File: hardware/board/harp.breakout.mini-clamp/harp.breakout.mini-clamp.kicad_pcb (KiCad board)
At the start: 2 copper layers, 40 x 75 mm, 16 parts, among them J1 Conn_01x12_Socket, J5 Conn_02x10_Odd_Even, J6 Conn_01x12_Socket, U5 TXB0108

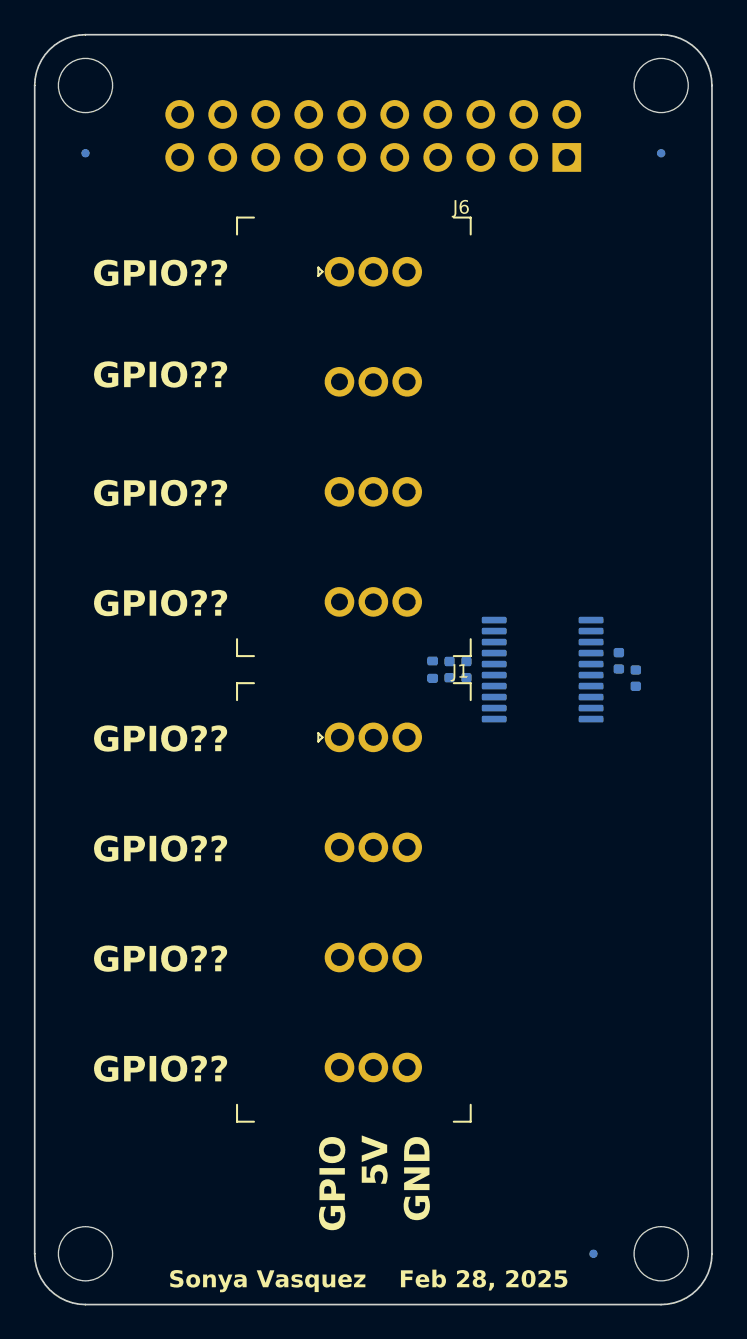
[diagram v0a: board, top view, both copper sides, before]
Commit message: route breakout board layout partially
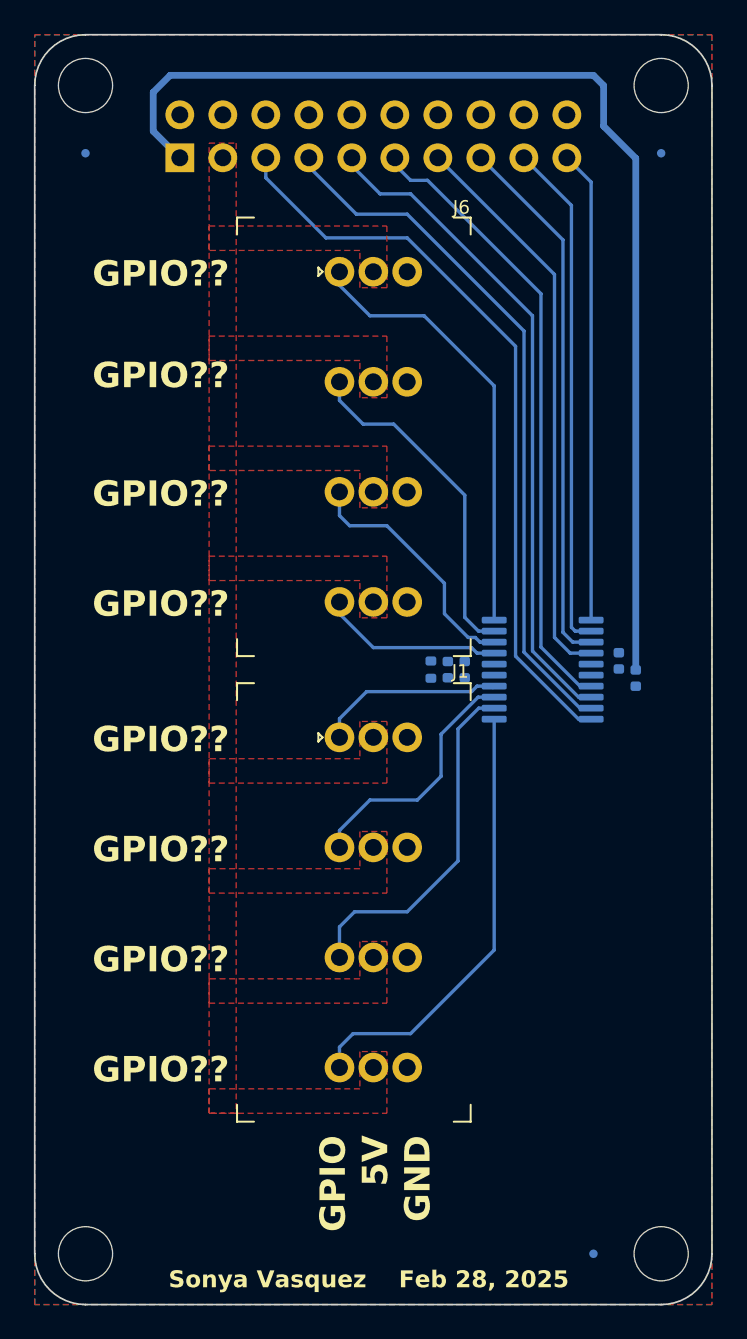
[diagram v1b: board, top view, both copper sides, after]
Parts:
- J5: footprint Connector_PinHeader_2.54mm:PinHeader_2x10_P2.54mm_Vertical -> Connector_PinSocket_2.54mm:PinSocket_2x10_P2.54mm_Vertical
- moved J5 22.9 mm to (128.6, 42.3), turned to -90 degrees
- moved C1 0.10 mm to (144.4, 72.5)
- moved C2 0.10 mm to (145.4, 72.5)
- moved R1 0.10 mm to (143.4, 72.5)
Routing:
- net +3.3V: track 0.00 -> 67.1 mm
- net /OUT3: track 0.00 -> 44.4 mm
- net /OUT2: track 0.00 -> 41.6 mm
- net /OUT1: track 0.00 -> 39.2 mm
- net /OUT0: track 0.00 -> 37.0 mm
- net /IN3: track 0.00 -> 33.7 mm
- net /IN2: track 0.00 -> 31.9 mm
- net /IN1: track 0.00 -> 30.1 mm
- net /IN0: track 0.00 -> 27.9 mm
- net /OUT3_5V: track 0.00 -> 26.4 mm
- net /IN0_5V: track 0.00 -> 26.2 mm
- net /OUT2_5V: track 0.00 -> 20.9 mm
- net /IN1_5V: track 0.00 -> 20.1 mm
- net /OUT1_5V: track 0.00 -> 14.9 mm
- net /IN2_5V: track 0.00 -> 14.7 mm
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- added copper zone on F.Cu, net +5V
- added copper zone on B.Cu, net GND
- added copper zone on F.Cu, net GND

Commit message: update breakout
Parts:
- added C5: 1uF, Capacitor_SMD:C_0402_1005Metric_Pad0.74x0.62mm_HandSolder, B.Cu at (155.0, 74.2)
- C1, C2, C3, C4: footprint Capacitor_SMD:C_0402_1005Metric -> Capacitor_SMD:C_0402_1005Metric_Pad0.74x0.62mm_HandSolder
- R1: footprint Resistor_SMD:R_0402_1005Metric -> Resistor_SMD:R_0402_1005Metric_Pad0.72x0.64mm_HandSolder
- moved FID2 61.0 mm to (123.0, 103.0)
- moved R1 11.6 mm to (155.0, 73.2), turned to 0 degrees
- moved C3 1.30 mm to (155.0, 71.8), turned to 180 degrees
- moved C4 1.28 mm to (155.0, 70.8), turned to 0 degrees
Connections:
- J1 pad 1: /OUT0_5V -> /IN3_5V
- J1 pad 10: /OUT3_5V -> /IN0_5V
- J1 pad 4: /OUT1_5V -> /IN2_5V
- J1 pad 7: /OUT2_5V -> /IN1_5V
- J5 pad 1: +3.3V -> /IN0
- J5 pad 11: /OUT0 -> /OUT1
- J5 pad 13: /IN3 -> /OUT2
- J5 pad 15: /IN2 -> /OUT3
- J5 pad 17: /IN1 -> +5V
- J5 pad 19: /IN0 -> +3.3V
- J5 pad 3: +5V -> /IN1
- J5 pad 5: /OUT3 -> /IN2
- J5 pad 7: /OUT2 -> /IN3
- J5 pad 9: /OUT1 -> /OUT0
- J6 pad 1: /IN0_5V -> /OUT3_5V
- J6 pad 10: /IN3_5V -> /OUT0_5V
- J6 pad 4: /IN1_5V -> /OUT2_5V
- J6 pad 7: /IN2_5V -> /OUT1_5V
- R1 pad 1: GND -> Net-(U5-OE)
- R1 pad 2: +5V -> +3.3V
- U5 pad 1: /IN0 -> /OUT3
- U5 pad 10: /OUT3 -> /IN0
- U5 pad 11: /OUT3_5V -> /IN0_5V
- U5 pad 12: /OUT2_5V -> /IN1_5V
- U5 pad 13: /OUT1_5V -> /IN2_5V
- U5 pad 14: /OUT0_5V -> /IN3_5V
- U5 pad 17: /IN3_5V -> /OUT0_5V
- U5 pad 18: /IN2_5V -> /OUT1_5V
- U5 pad 19: /IN1_5V -> /OUT2_5V
- U5 pad 2: /IN1 -> /OUT2
- U5 pad 20: /IN0_5V -> /OUT3_5V
- U5 pad 3: /IN2 -> /OUT1
- U5 pad 4: /IN3 -> /OUT0
- U5 pad 5: +3V3 -> +3.3V
- U5 pad 6: +3V3 -> Net-(U5-OE)
- U5 pad 7: /OUT0 -> /IN3
- U5 pad 8: /OUT1 -> /IN2
- U5 pad 9: /OUT2 -> /IN1
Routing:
- net +3.3V: track 67.1 -> 34.6 mm
- net /IN0: track 27.9 -> 49.5 mm
- net /IN1: track 30.1 -> 46.4 mm
- net /OUT3: track 44.4 -> 30.0 mm
- net /IN2: track 31.9 -> 43.8 mm
- net /OUT2: track 41.6 -> 32.4 mm
- net /IN3: track 33.7 -> 41.8 mm
- net /OUT1: track 39.2 -> 35.4 mm
- net GND: track 0.00 -> 3.51 mm, vias 0 -> 4
- net Net-(U5-OE): track 0.00 -> 2.85 mm
- net /OUT0: track 37.0 -> 38.1 mm
- net /OUT2_5V: track 20.9 -> 20.1 mm
- net +5V: vias 0 -> 2
- added copper zone on B.Cu, net +5V
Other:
- board text added: "0368-E-002-001.000.000"
- board text added: "AUX GPIO Breakout"
- board text added: "Sonya Vasquez Mar 3, 2025"
- board text removed: "GPIO??"
- board text removed: "Sonya Vasquez Feb 28, 2025"

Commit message: update breakout board silk
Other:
- board text added: "· 5V logic input/output. · connected devices using pullups must use pullups >50KOhm. · compatible connectors: 3M Mini Clamp Socket Series. · 37103-2165-000 FL 100 · 37103-3101-000 FL 100"
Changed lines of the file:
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@@
 		(pad_to_mask_clearance 0)
 		(allow_soldermask_bridges_in_footprints no)
+		(aux_axis_origin 120 110)
+		(grid_origin 120 110)
 		(pcbplotparams
 			(layerselection 0x00010fc_ffffffff)
 			(plot_on_all_layers_selection 0x0000000_00000000)
 			(disableapertmacros no)
-			(usegerberextensions no)
-			(usegerberattributes yes)
+			(usegerberextensions yes)
+			(usegerberattributes no)
 			(usegerberadvancedattributes yes)
 			(creategerberjobfile yes)
@@
 			(viasonmask no)
 			(mode 1)
-			(useauxorigin no)
+			(useauxorigin yes)
 			(hpglpennumber 1)
 			(hpglpenspeed 20)
@@
 			(outputformat 1)
 			(mirror no)
-			(drillshape 1)
+			(drillshape 0)
 			(scaleselection 1)
-			(outputdirectory "")
+			(outputdirectory "exports/gerbers/")
 		)
 	)
@@
 		)
 	)
+	(gr_text "· 5V logic input/output.\n· connected devices using pullups must use pullups >50KOhm.\n· compatible connectors: 3M Mini Clamp Socket Series.\n  · 37103-2165-000 FL 100\n  · 37103-3101-000 FL 100"
+		(at 129.2 49.5 90)
+		(layer "B.SilkS")
+		(effects
+			(font
+				(size 1 1)
+				(thickness 0.2)
+				(bold yes)
+			)
+			(justify left bottom mirror)
+		)
+	)
 	(gr_text "GPIO26"
 		(at 139.992 48.2 90)
@@
 	)
 	(gr_text "GPIO"
-		(at 137 105.3 -90)
+		(at 137 105.3 270)
 		(layer "F.SilkS")
 		(effects
@@
 	)
 	(gr_text "AUX GPIO Breakout"
-		(at 156.7 61.2 -90)
+		(at 156.7 61.2 270)
 		(layer "F.SilkS")
 		(effects
